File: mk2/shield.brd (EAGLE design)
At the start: 83.8 x 55.9 mm, 51 parts, among them P0 CON_DIL_20, P1 CON_DIL_20, P2 CON_DIL_20, P3 CON_DIL_20, P4 CON_DIL_20, P5 CON_DIL_20, Q1 20M

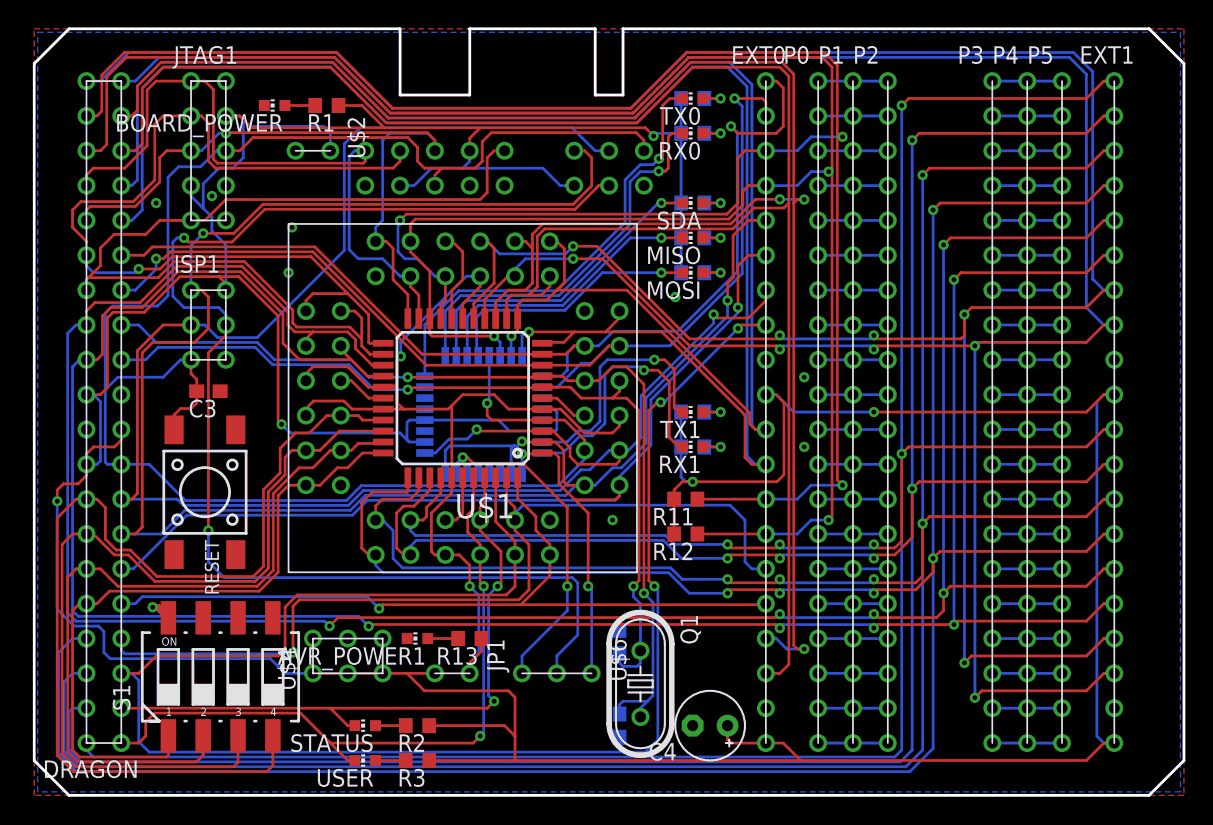
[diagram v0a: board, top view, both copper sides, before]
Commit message: [mk2 reset separation]
	- split the jtag and isp connectors such that
		- isp is connected to the atmega88 and the external isp
		- jtat is connected to the atmega1284 and the external jtag
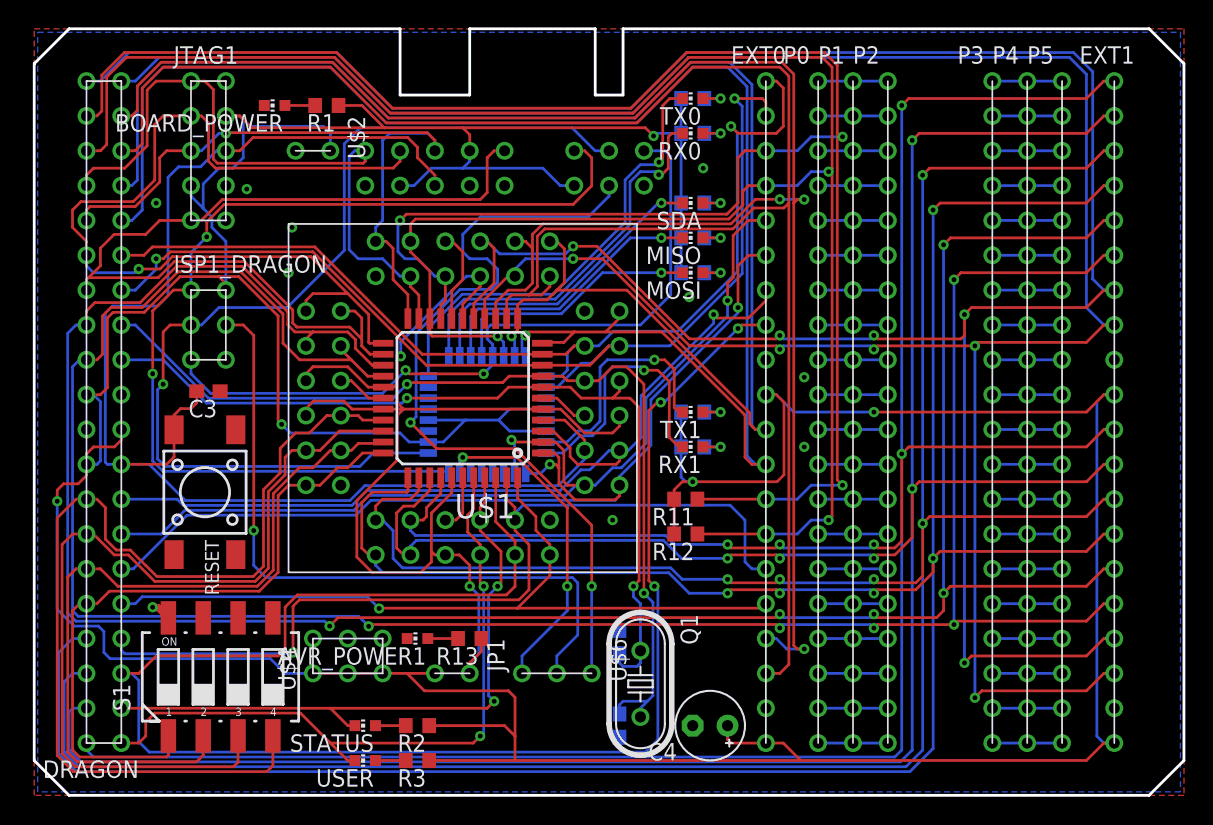
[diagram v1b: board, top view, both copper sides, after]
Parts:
- moved U$5 0.25 mm to (34.3, 34.1)
- renumbered ISP1 to ISP1_DRAGON, ISP2 to ISP2_EXT
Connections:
- net MOSI_MEGA88 renamed MOSI_88
- removed net /RESET: C3.2, DRAGON.P$9, ISP1_DRAGON.P$3, ISP2_EXT.P$3, JTAG1.P$8, JTAG2.P$8, RESET.3, U$1.4, U$3.P$4, U$5.29
- removed net MISO: DRAGON.P$7, EXT0.P$5, ISP1_DRAGON.P$1, ISP2_EXT.P$1, U$1.2, U$3.P$2, U$5.10, U$5.16
- removed net MOSI: ISP1_DRAGON.P$5, ISP2_EXT.P$5, U$6.P$2
- removed net MOSI_MEGA1284: DRAGON.P$6, EXT0.P$6, U$1.1, U$3.P$1, U$5.9, U$6.P$1
- removed net SCK: DRAGON.P$8, EXT0.P$7, ISP1_DRAGON.P$2, ISP2_EXT.P$2, U$1.3, U$3.P$3, U$5.17
- new net /RESET_1284: C3.2, DRAGON.P$9, JTAG1.P$8, JTAG2.P$8, RESET.3, U$1.4, U$3.P$4
- new net /RESET_88: ISP1_DRAGON.P$3, ISP2_EXT.P$3, U$5.29
- new net MISO_1284: DRAGON.P$7, EXT0.P$5, U$1.2, U$3.P$2, U$5.10
- new net MISO_88: ISP1_DRAGON.P$1, ISP2_EXT.P$1, U$5.16
- new net MOSI_1284: DRAGON.P$6, EXT0.P$6, U$1.1, U$3.P$1, U$5.9
- new net MOSI_DRAGON: ISP1_DRAGON.P$5, U$6.P$2
- new net MOSI_EXT: ISP2_EXT.P$5, U$6.P$1
- new net SCK_1284: DRAGON.P$8, EXT0.P$7, U$1.3, U$3.P$3
- new net SCK_88: ISP1_DRAGON.P$2, ISP2_EXT.P$2, U$5.17
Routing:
- net MISO: track 140.0 -> 0.00 mm, vias 3 -> 0
- net SCK: track 132.6 -> 0.00 mm, vias 2 -> 0
- net /RESET: track 131.0 -> 0.00 mm, vias 1 -> 0
- net /RESET_1284: track 0.00 -> 100.0 mm
- net MOSI: track 95.5 -> 0.00 mm, vias 2 -> 0
- net MOSI_MEGA1284: track 86.4 -> 0.00 mm, vias 3 -> 0
- net MISO_88: track 0.00 -> 74.5 mm, vias 0 -> 2
- net SCK_88: track 0.00 -> 73.7 mm, vias 0 -> 1
- net MOSI_1284: track 0.00 -> 73.1 mm, vias 0 -> 2
- net MISO_1284: track 0.00 -> 72.2 mm, vias 0 -> 2
- net SCK_1284: track 0.00 -> 64.4 mm, vias 0 -> 1
- net MOSI_EXT: track 0.00 -> 59.1 mm, vias 0 -> 2
- net /RESET_88: track 0.00 -> 54.1 mm, vias 0 -> 2
- net MOSI_DRAGON: track 0.00 -> 50.5 mm, vias 0 -> 1
- net VCC_MEGA1284: track 76.9 -> 89.9 mm
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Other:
- board text added: "EXTERN"
- board text added: "MEGA88"
- board text removed: "LED"
- board text removed: "MAIN"
